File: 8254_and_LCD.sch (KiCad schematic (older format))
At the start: 7 parts, among them U2 PAL16L8, U3 8254

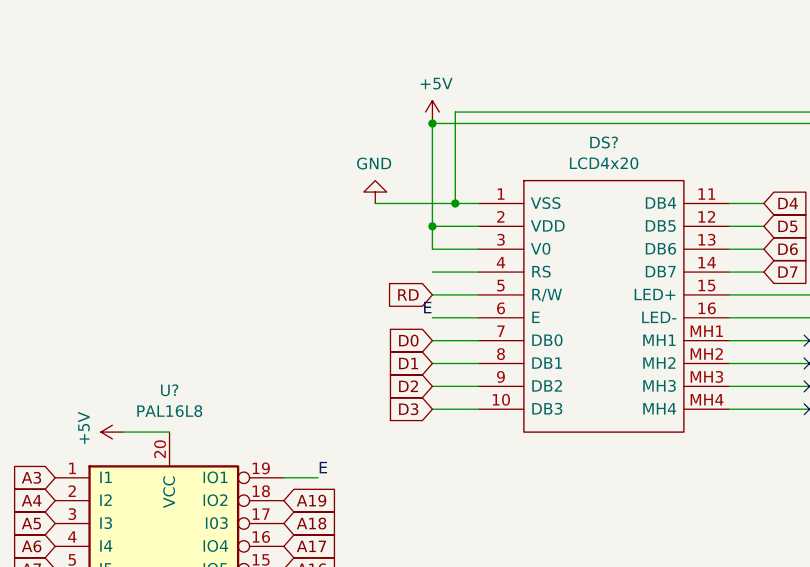
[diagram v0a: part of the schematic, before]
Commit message: updated 8254 and LCD file
Fixed the A1->RS and A2->R/W
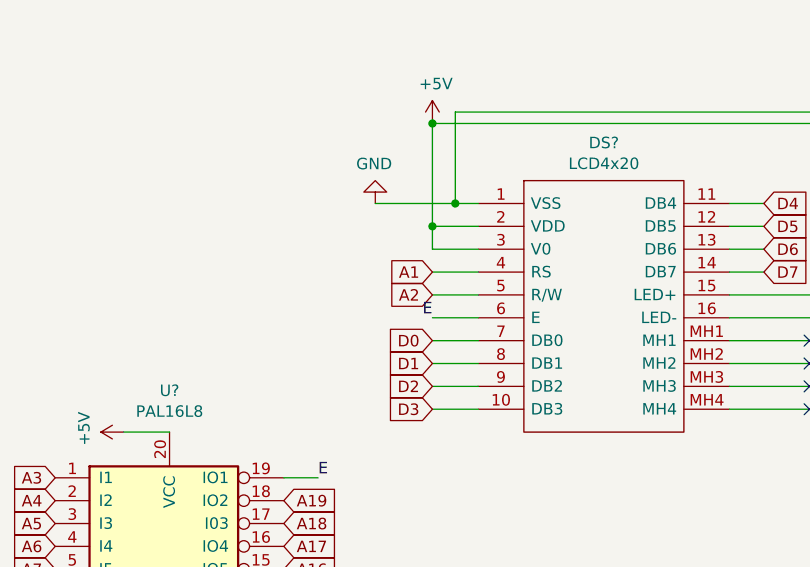
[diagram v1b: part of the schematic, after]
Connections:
- net labels removed: RD
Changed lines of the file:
@@
 Text GLabel 9300 3000 2    50   Input ~ 0
 D7
-Text GLabel 7850 3100 0    50   Input ~ 0
-RD
 $Comp
 L power:+5V #PWR?
@@
 Text GLabel 7200 4000 2    50   Input ~ 0
 A19
+Text GLabel 7850 3000 0    50   Input ~ 0
+A1
+Text GLabel 7850 3100 0    50   Input ~ 0
+A2
 $EndSCHEMATC

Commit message: cleaned up
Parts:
- renumbered U3 to U?, U2 to U?
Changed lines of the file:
@@
 $Descr A4 11693 8268
 encoding utf-8
-Sheet 1 1
+Sheet 5 5
 Title ""
 Date ""
@@
 	2700 3150 2700 3350
 $Comp
-L power:GND #PWR0102
+L power:GND #PWR?
 U 1 1 60792917
 P 2700 3350
-F 0 "#PWR0102" H 2700 3100 50  0001 C CNN
+F 0 "#PWR?" H 2700 3100 50  0001 C CNN
 F 1 "GND" H 2705 3177 50  0000 C CNN
 F 2 "" H 2700 3350 50  0001 C CNN
@@
 $EndComp
 $Comp
-L Timer:8254 U3
+L Timer:8254 U?
 U 1 1 6078D3E6
 P 2700 2150
-F 0 "U3" H 2700 3331 50  0000 C CNN
+F 0 "U?" H 2700 3331 50  0000 C CNN
 F 1 "8254" H 2700 3240 50  0000 C CNN
 F 2 "Package_DIP:DIP-24_W15.24mm" H 2750 2400 50  0001 C CNN
@@
 D7
 $Comp
-L power:+5V #PWR0101
+L power:+5V #PWR?
 U 1 1 607903CC
 P 2700 850
-F 0 "#PWR0101" H 2700 700 50  0001 C CNN
+F 0 "#PWR?" H 2700 700 50  0001 C CNN
 F 1 "+5V" H 2715 1023 50  0000 C CNN
 F 2 "" H 2700 850 50  0001 C CNN
@@
 	2000 2850 2000 3700
 $Comp
-L Logic_Programmable:PAL16L8 U2
+L Logic_Programmable:PAL16L8 U?
 U 1 1 60874ABA
 P 1500 4200
-F 0 "U2" H 1500 5081 50  0000 C CNN
+F 0 "U?" H 1500 5081 50  0000 C CNN
 F 1 "PAL16L8" H 1500 4990 50  0000 C CNN
 F 2 "" H 1500 4200 50  0001 C CNN

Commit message: tweaked a few things
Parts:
- gave numbers to parts that had none: 7
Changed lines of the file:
@@
 	7850 2350 7850 2800
 $Comp
-L power:+5V #PWR?
+L power:+5V #PWR0149
 U 1 1 608AC27A
 P 7850 2350
-F 0 "#PWR?" H 7850 2200 50  0001 C CNN
+F 0 "#PWR0149" H 7850 2200 50  0001 C CNN
 F 1 "+5V" H 7865 2523 50  0000 C CNN
 F 2 "" H 7850 2350 50  0001 C CNN
@@
 $EndComp
 $Comp
-L power:GND #PWR?
+L power:GND #PWR0150
 U 1 1 608A9C65
 P 7600 2700
-F 0 "#PWR?" H 7600 2450 50  0001 C CNN
+F 0 "#PWR0150" H 7600 2450 50  0001 C CNN
 F 1 "GND" H 7605 2527 50  0000 C CNN
 F 2 "" H 7600 2700 50  0001 C CNN
@@
 	2700 3150 2700 3350
 $Comp
-L power:GND #PWR?
+L power:GND #PWR0151
 U 1 1 60792917
 P 2700 3350
-F 0 "#PWR?" H 2700 3100 50  0001 C CNN
+F 0 "#PWR0151" H 2700 3100 50  0001 C CNN
 F 1 "GND" H 2705 3177 50  0000 C CNN
 F 2 "" H 2700 3350 50  0001 C CNN
@@
 	3300 2550 4050 2550
 $Comp
-L Connector:Conn_01x03_Male J?
+L Connector:Conn_01x03_Male J503
 U 1 1 608DA5FE
 P 4250 2650
-F 0 "J?" H 4358 2931 50  0000 C CNN
+F 0 "J503" H 4358 2931 50  0000 C CNN
 F 1 "Conn_01x03_Male" H 4358 2840 50  0000 C CNN
 F 2 "" H 4250 2650 50  0001 C CNN
@@
 	3300 2050 4050 2050
 $Comp
-L Connector:Conn_01x02_Male J?
+L Connector:Conn_01x02_Male J502
 U 1 1 608D6258
 P 4250 2050
-F 0 "J?" H 4358 2231 50  0000 C CNN
+F 0 "J502" H 4358 2231 50  0000 C CNN
 F 1 "Conn_01x02_Male" H 4358 2140 50  0000 C CNN
 F 2 "" H 4250 2050 50  0001 C CNN
@@
 	3300 1550 4050 1550
 $Comp
-L Connector:Conn_01x03_Male J?
+L Connector:Conn_01x03_Male J501
 U 1 1 608CD19D
 P 4250 1650
-F 0 "J?" H 4222 1674 50  0000 R CNN
+F 0 "J501" H 4222 1674 50  0000 R CNN
 F 1 "Conn_01x03_Male" H 4222 1583 50  0000 R CNN
 F 2 "" H 4250 1650 50  0001 C CNN
@@
 $EndComp
 $Comp
-L Timer:8254 U?
+L Timer:8254 U502
 U 1 1 6078D3E6
 P 2700 2150
-F 0 "U?" H 2700 3331 50  0000 C CNN
+F 0 "U502" H 2700 3331 50  0000 C CNN
 F 1 "8254" H 2700 3240 50  0000 C CNN
 F 2 "Package_DIP:DIP-24_W15.24mm" H 2750 2400 50  0001 C CNN
@@
 D7
 $Comp
-L power:+5V #PWR?
+L power:+5V #PWR0152
 U 1 1 607903CC
 P 2700 850
-F 0 "#PWR?" H 2700 700 50  0001 C CNN
+F 0 "#PWR0152" H 2700 700 50  0001 C CNN
 F 1 "+5V" H 2715 1023 50  0000 C CNN
 F 2 "" H 2700 850 50  0001 C CNN
@@
 	9150 2700 9300 2700
 $Comp
-L LCD4x20:LCD4x20 DS?
+L LCD4x20:LCD4x20 DS501
 U 1 1 608A6AEF
 P 8050 2700
-F 0 "DS?" H 8600 2965 50  0000 C CNN
+F 0 "DS501" H 8600 2965 50  0000 C CNN
 F 1 "LCD4x20" H 8600 2874 50  0000 C CNN
 F 2 "LCD4x20" H 9000 2800 50  0001 L CNN
@@
 A3
 $Comp
-L Logic_Programmable:PAL16L8 U?
+L Logic_Programmable:PAL16L8 U503
 U 1 1 6097CD3F
 P 6700 4400
-F 0 "U?" H 6700 5281 50  0000 C CNN
+F 0 "U503" H 6700 5281 50  0000 C CNN
 F 1 "PAL16L8" H 6700 5190 50  0000 C CNN
 F 2 "" H 6700 4400 50  0001 C CNN
@@
 	7200 3900 7350 3900
 $Comp
-L power:GND #PWR?
+L power:GND #PWR0153
 U 1 1 60984E31
 P 6700 5000
-F 0 "#PWR?" H 6700 4750 50  0001 C CNN
+F 0 "#PWR0153" H 6700 4750 50  0001 C CNN
 F 1 "GND" H 6705 4827 50  0000 C CNN
 F 2 "" H 6700 5000 50  0001 C CNN
@@
 	1500 3500 1350 3500
 $Comp
-L power:GND #PWR?
+L power:GND #PWR0154
 U 1 1 60997570
 P 1500 4800
-F 0 "#PWR?" H 1500 4550 50  0001 C CNN
+F 0 "#PWR0154" H 1500 4550 50  0001 C CNN
 F 1 "GND" H 1505 4627 50  0000 C CNN
 F 2 "" H 1500 4800 50  0001 C CNN
@@
 D7
 $Comp
-L power:+5V #PWR?
+L power:+5V #PWR0155
 U 1 1 60A1CF5F
 P 1350 3500
-F 0 "#PWR?" H 1350 3350 50  0001 C CNN
+F 0 "#PWR0155" H 1350 3350 50  0001 C CNN
 F 1 "+5V" H 1365 3673 50  0000 C CNN
 F 2 "" H 1350 3500 50  0001 C CNN
@@
 $EndComp
 $Comp
-L power:+5V #PWR?
+L power:+5V #PWR0156
 U 1 1 60A25246
 P 6500 3700
-F 0 "#PWR?" H 6500 3550 50  0001 C CNN
+F 0 "#PWR0156" H 6500 3550 50  0001 C CNN
 F 1 "+5V" H 6515 3873 50  0000 C CNN
 F 2 "" H 6500 3700 50  0001 C CNN
@@
 	2000 2850 2000 3700
 $Comp
-L Logic_Programmable:PAL16L8 U?
+L Logic_Programmable:PAL16L8 U501
 U 1 1 60874ABA
 P 1500 4200
-F 0 "U?" H 1500 5081 50  0000 C CNN
+F 0 "U501" H 1500 5081 50  0000 C CNN
 F 1 "PAL16L8" H 1500 4990 50  0000 C CNN
 F 2 "" H 1500 4200 50  0001 C CNN

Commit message: made some modifications
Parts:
- added U? (x2): 74AHC1G08, symbol 74xGxx:74AHC1G08
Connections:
- wire segments 58 -> 64
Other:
- moved on the sheet: DS501, J501, J502, J503, U501, U502, U503

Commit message: made final adjustments to all the designes
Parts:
- removed U? (x2): 74AHC1G08, symbol 74xGxx:74AHC1G08
- added C501: 0.1uF, Capacitor_SMD:CP_Elec_3x5.3, symbol Device:C
- added U501: 74LS08, Package_DIP:DIP-14_W7.62mm_SMDSocket_SmallPads, symbol 74xx:74LS08
- DS501: footprint LCD4x20 -> parts:LCD4x20
- J501, J503: footprint (none) -> Connector_JST:JST_GH_BM03B-GHS-TBT_1x03-1MP_P1.25mm_Vertical
- J502: footprint (none) -> Connector_JST:JST_GH_BM02B-GHS-TBT_1x02-1MP_P1.25mm_Vertical
- U502: renamed from U501; footprint (none) -> Package_DIP:DIP-20_W7.62mm_SMDSocket_SmallPads
- U504: renamed from U503; footprint (none) -> Package_DIP:DIP-20_W7.62mm_SMDSocket_SmallPads
- renumbered U502 to U503
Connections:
- net labels added: VCC
- wire segments 64 -> 63
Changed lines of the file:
@@
 $Descr A4 11693 8268
 encoding utf-8
-Sheet 5 6
+Sheet 5 8
 Title ""
 Date ""
@@
 	7000 2300 7000 2750
 $Comp
-L power:+5V #PWR0149
-U 1 1 608AC27A
-P 7000 2300
-F 0 "#PWR0149" H 7000 2150 50  0001 C CNN
-F 1 "+5V" H 7015 2473 50  0000 C CNN
-F 2 "" H 7000 2300 50  0001 C CNN
-F 3 "" H 7000 2300 50  0001 C CNN
-	1    7000 2300
-	1    0    0    -1
-$EndComp
-$Comp
-L power:GND #PWR0150
+L power:GND #PWR0510
 U 1 1 608A9C65
 P 6750 2650
-F 0 "#PWR0150" H 6750 2400 50  0001 C CNN
+F 0 "#PWR0510" H 6750 2400 50  0001 C CNN
 F 1 "GND" H 6755 2477 50  0000 C CNN
 F 2 "" H 6750 2650 50  0001 C CNN
@@
 	3750 2850 3750 3050
 $Comp
-L power:GND #PWR0151
+L power:GND #PWR0506
 U 1 1 60792917
 P 3750 3050
-F 0 "#PWR0151" H 3750 2800 50  0001 C CNN
+F 0 "#PWR0506" H 3750 2800 50  0001 C CNN
 F 1 "GND" H 3755 2877 50  0000 C CNN
 F 2 "" H 3750 3050 50  0001 C CNN
@@
 F 0 "J503" H 5408 2631 50  0000 C CNN
 F 1 "Conn_01x03_Male" H 5408 2540 50  0000 C CNN
-F 2 "" H 5300 2350 50  0001 C CNN
+F 2 "Connector_JST:JST_GH_BM03B-GHS-TBT_1x03-1MP_P1.25mm_Vertical" H 5300 2350 50  0001 C CNN
 F 3 "~" H 5300 2350 50  0001 C CNN
 	1    5300 2350
@@
 F 0 "J502" H 5408 1931 50  0000 C CNN
 F 1 "Conn_01x02_Male" H 5408 1840 50  0000 C CNN
-F 2 "" H 5300 1750 50  0001 C CNN
+F 2 "Connector_JST:JST_GH_BM02B-GHS-TBT_1x02-1MP_P1.25mm_Vertical" H 5300 1750 50  0001 C CNN
 F 3 "~" H 5300 1750 50  0001 C CNN
 	1    5300 1750
@@
 F 0 "J501" H 5272 1374 50  0000 R CNN
 F 1 "Conn_01x03_Male" H 5272 1283 50  0000 R CNN
-F 2 "" H 5300 1350 50  0001 C CNN
+F 2 "Connector_JST:JST_GH_BM03B-GHS-TBT_1x03-1MP_P1.25mm_Vertical" H 5300 1350 50  0001 C CNN
 F 3 "~" H 5300 1350 50  0001 C CNN
 	1    5300 1350
@@
 $EndComp
 $Comp
-L Timer:8254 U502
+L Timer:8254 U503
 U 1 1 6078D3E6
 P 3750 1850
-F 0 "U502" H 3750 3031 50  0000 C CNN
+F 0 "U503" H 3750 3031 50  0000 C CNN
 F 1 "8254" H 3750 2940 50  0000 C CNN
 F 2 "Package_DIP:DIP-24_W15.24mm" H 3800 2100 50  0001 C CNN
@@
 	1    0    0    -1
 $EndComp
-Wire Wire Line
-	3750 550  3750 850
 Text Label 2700 1850 0    50   ~ 0
 D7
@@
 Text Label 2700 1150 0    50   ~ 0
 D0
-Text Label 2300 2250 0    50   ~ 0
-A0
-Text Label 2300 2350 0    50   ~ 0
-A1
 Wire Wire Line
 	3150 1150 2700 1150
@@
 Text GLabel 2700 1850 0    50   Input ~ 0
 D7
-$Comp
-L power:+5V #PWR0152
-U 1 1 607903CC
-P 3750 550
-F 0 "#PWR0152" H 3750 400 50  0001 C CNN
-F 1 "+5V" H 3765 723 50  0000 C CNN
-F 2 "" H 3750 550 50  0001 C CNN
-F 3 "" H 3750 550 50  0001 C CNN
-	1    3750 550
-	1    0    0    -1
-$EndComp
-Connection ~ 7000 2300
 NoConn ~ 8650 3550
 NoConn ~ 8650 3450
@@
 F 0 "DS501" H 7750 2915 50  0000 C CNN
 F 1 "LCD4x20" H 7750 2824 50  0000 C CNN
-F 2 "LCD4x20" H 8150 2750 50  0001 L CNN
+F 2 "parts:LCD4x20" H 8150 2750 50  0001 L CNN
 F 3 "https://componentsearchengine.com/Datasheets/1/LCD4x20.pdf" H 8150 2650 50  0001 L CNN
 F 4 "LCD Character Display Modules & Accessories STN-Y/G Transfl 77.5 x 47.0" H 8150 2550 50  0001 L CNN "Description"
@@
 	7200 3550 7000 3550
 $Comp
-L Logic_Programmable:PAL16L8 U503
+L Logic_Programmable:PAL16L8 U504
 U 1 1 6097CD3F
 P 6500 4650
-F 0 "U503" H 6500 5531 50  0000 C CNN
+F 0 "U504" H 6500 5531 50  0000 C CNN
 F 1 "PAL16L8" H 6500 5440 50  0000 C CNN
-F 2 "" H 6500 4650 50  0001 C CNN
+F 2 "Package_DIP:DIP-20_W7.62mm_SMDSocket_SmallPads" H 6500 4650 50  0001 C CNN
 F 3 "" H 6500 4650 50  0001 C CNN
 	1    6500 4650
@@
 	7000 4150 7150 4150
 $Comp
-L power:GND #PWR0153
+L power:GND #PWR0509
 U 1 1 60984E31
 P 6500 5250
-F 0 "#PWR0153" H 6500 5000 50  0001 C CNN
+F 0 "#PWR0509" H 6500 5000 50  0001 C CNN
 F 1 "GND" H 6505 5077 50  0000 C CNN
 F 2 "" H 6500 5250 50  0001 C CNN
@@
 	2550 3200 2400 3200
 $Comp
-L power:GND #PWR0154
+L power:GND #PWR0504
 U 1 1 60997570
 P 2550 4500
-F 0 "#PWR0154" H 2550 4250 50  0001 C CNN
+F 0 "#PWR0504" H 2550 4250 50  0001 C CNN
 F 1 "GND" H 2555 4327 50  0000 C CNN
 F 2 "" H 2550 4500 50  0001 C CNN
@@
 D7
 $Comp
-L power:+5V #PWR0155
+L power:+5V #PWR0503
 U 1 1 60A1CF5F
 P 2400 3200
-F 0 "#PWR0155" H 2400 3050 50  0001 C CNN
+F 0 "#PWR0503" H 2400 3050 50  0001 C CNN
 F 1 "+5V" H 2415 3373 50  0000 C CNN
 F 2 "" H 2400 3200 50  0001 C CNN
@@
 	0    -1   1    0
 $EndComp
-$Comp
-L power:+5V #PWR0156
-U 1 1 60A25246
-P 6300 3950
-F 0 "#PWR0156" H 6300 3800 50  0001 C CNN
-F 1 "+5V" H 6315 4123 50  0000 C CNN
-F 2 "" H 6300 3950 50  0001 C CNN
-F 3 "" H 6300 3950 50  0001 C CNN
-	1    6300 3950
-	0    -1   -1   0
-$EndComp
 Wire Wire Line
 	3050 2550 3050 3400
 $Comp
-L Logic_Programmable:PAL16L8 U501
+L Logic_Programmable:PAL16L8 U502
 U 1 1 60874ABA
 P 2550 3900
-F 0 "U501" H 2550 4781 50  0000 C CNN
+F 0 "U502" H 2550 4781 50  0000 C CNN
 F 1 "PAL16L8" H 2550 4690 50  0000 C CNN
-F 2 "" H 2550 3900 50  0001 C CNN
+F 2 "Package_DIP:DIP-20_W7.62mm_SMDSocket_SmallPads" H 2550 3900 50  0001 C CNN
 F 3 "" H 2550 3900 50  0001 C CNN
 	1    2550 3900
@@
 Text GLabel 7000 3050 0    50   Input ~ 0
 A2
-Text GLabel 2050 5050 0    50   Input ~ 0
+Text GLabel 5850 5700 0    50   Input ~ 0
 A18
-Text GLabel 2050 5150 0    50   Input ~ 0
+Text GLabel 5850 5900 0    50   Input ~ 0
 A19
-$Comp
-L 74xGxx:74AHC1G08 U?
-U 1 1 60BF9FD9
-P 2350 5100
-F 0 "U?" H 2325 5367 50  0000 C CNN
-F 1 "74AHC1G08" H 2325 5276 50  0000 C CNN
-F 2 "" H 2350 5100 50  0001 C CNN
-F 3 "http://www.ti.com/lit/sg/scyt129e/scyt129e.pdf" H 2350 5100 50  0001 C CNN
-	1    2350 5100
-	1    0    0    -1
-$EndComp
-Text GLabel 5900 5750 0    50   Input ~ 0
-A18
-Text GLabel 5900 5850 0    50   Input ~ 0
-A19
-$Comp
-L 74xGxx:74AHC1G08 U?
-U 1 1 60C02507
-P 6200 5800
-F 0 "U?" H 6175 6067 50  0000 C CNN
-F 1 "74AHC1G08" H 6175 5976 50  0000 C CNN
-F 2 "" H 6200 5800 50  0001 C CNN
-F 3 "http://www.ti.com/lit/sg/scyt129e/scyt129e.pdf" H 6200 5800 50  0001 C CNN
-	1    6200 5800
-	1    0    0    -1
-$EndComp
 Wire Wire Line
 	3050 3500 3400 3500
@@
 Wire Wire Line
 	6450 5800 7300 5800
+Text GLabel 2000 5000 0    50   Input ~ 0
+A18
+Text GLabel 2000 5200 0    50   Input ~ 0
+A19
+$Comp
+L 74xx:74LS08 U501
+U 1 1 61076578
+P 2300 5100
+F 0 "U501" H 2300 5425 50  0000 C CNN
+F 1 "74LS08" H 2300 5334 50  0000 C CNN
+F 2 "Package_DIP:DIP-14_W7.62mm_SMDSocket_SmallPads" H 2300 5100 50  0001 C CNN
+F 3 "http://www.ti.com/lit/gpn/sn74LS08" H 2300 5100 50  0001 C CNN
+	1    2300 5100
+	1    0    0    -1
+$EndComp
+$Comp
+L Device:C C?
+U 1 1 6108FD70
+P 3900 850
+AR Path="/6108FD70" Ref="C?"  Part="1"
+AR Path="/6095B35F/6108FD70" Ref="C501"  Part="1"
+F 0 "C501" H 4015 896 50  0000 L CNN
+F 1 "0.1uF" H 4015 805 50  0000 L CNN
+F 2 "Capacitor_SMD:CP_Elec_3x5.3" H 3938 700 50  0001 C CNN
+F 3 "~" H 3900 850 50  0001 C CNN
+	1    3900 850
+	0    1    1    0
+$EndComp
+$Comp
+L power:GND #PWR?
+U 1 1 6108FD76
+P 4050 850
+AR Path="/6108FD76" Ref="#PWR?"  Part="1"
+AR Path="/6095B35F/6108FD76" Ref="#PWR0507"  Part="1"
+F 0 "#PWR0507" H 4050 600 50  0001 C CNN
+F 1 "GND" H 4055 677 50  0000 C CNN
+F 2 "" H 4050 850 50  0001 C CNN
+F 3 "" H 4050 850 50  0001 C CNN
+	1    4050 850
+	0    -1   -1   0
+$EndComp
+$Comp
+L power:VCC #PWR0505
+U 1 1 6137586E
+P 3750 850
+F 0 "#PWR0505" H 3750 700 50  0001 C CNN
+F 1 "VCC" V 3765 977 50  0000 L CNN
+F 2 "" H 3750 850 50  0001 C CNN
+F 3 "" H 3750 850 50  0001 C CNN
+	1    3750 850
+	0    -1   -1   0
+$EndComp
+Connection ~ 3750 850
+$Comp
+L power:VCC #PWR0508
+U 1 1 613780DF
+P 6300 3950
+F 0 "#PWR0508" H 6300 3800 50  0001 C CNN
+F 1 "VCC" V 6315 4077 50  0000 L CNN
+F 2 "" H 6300 3950 50  0001 C CNN
+F 3 "" H 6300 3950 50  0001 C CNN
+	1    6300 3950
+	0    -1   -1   0
+$EndComp
+$Comp
+L power:VCC #PWR0511
+U 1 1 6137BA70
+P 7000 2300
+F 0 "#PWR0511" H 7000 2150 50  0001 C CNN
+F 1 "VCC" H 7015 2473 50  0000 C CNN
+F 2 "" H 7000 2300 50  0001 C CNN
+F 3 "" H 7000 2300 50  0001 C CNN
+	1    7000 2300
+	1    0    0    -1
+$EndComp
+Connection ~ 7000 2300
+$Comp
+L 74xx:74LS08 U501
+U 5 1 61452EC9
+P 1100 5350
+F 0 "U501" H 1330 5396 50  0000 L CNN
+F 1 "74LS08" H 1330 5305 50  0000 L CNN
+F 2 "Package_DIP:DIP-14_W7.62mm_SMDSocket_SmallPads" H 1100 5350 50  0001 C CNN
+F 3 "http://www.ti.com/lit/gpn/sn74LS08" H 1100 5350 50  0001 C CNN
+	5    1100 5350
+	1    0    0    -1
+$EndComp
+$Comp
+L power:VCC #PWR0501
+U 1 1 61455BF9
+P 1100 4850
+F 0 "#PWR0501" H 1100 4700 50  0001 C CNN
+F 1 "VCC" H 1115 5023 50  0000 C CNN
+F 2 "" H 1100 4850 50  0001 C CNN
+F 3 "" H 1100 4850 50  0001 C CNN
+	1    1100 4850
+	1    0    0    -1
+$EndComp
+$Comp
+L power:GND #PWR0502
+U 1 1 61456444
+P 1100 5850
+F 0 "#PWR0502" H 1100 5600 50  0001 C CNN
+F 1 "GND" H 1105 5677 50  0000 C CNN
+F 2 "" H 1100 5850 50  0001 C CNN
+F 3 "" H 1100 5850 50  0001 C CNN
+	1    1100 5850
+	1    0    0    -1
+$EndComp
+$Comp
+L 74xx:74LS08 U501
+U 2 1 61458D64
+P 6150 5800
+F 0 "U501" H 6150 6125 50  0000 C CNN
+F 1 "74LS08" H 6150 6034 50  0000 C CNN
+F 2 "Package_DIP:DIP-14_W7.62mm_SMDSocket_SmallPads" H 6150 5800 50  0001 C CNN
+F 3 "http://www.ti.com/lit/gpn/sn74LS08" H 6150 5800 50  0001 C CNN
+	2    6150 5800
+	1    0    0    -1
+$EndComp
 $EndSCHEMATC
